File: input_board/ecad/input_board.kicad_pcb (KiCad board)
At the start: 2 copper layers, 165.2 x 98.2 mm, 165 parts, among them J1 Conn_01x03_Male, J10 Conn_01x02_Female, J11 Conn_01x02_Female, J12 Conn_01x02_Female, J13 Conn_01x02_Female, J14 Conn_01x02_Female, J15 Conn_01x02_Female, J2 RCJ-041, J3 RCJ-041, J4 Conn_01x04_Female, J5 Conn_01x02_Female, J6 Conn_01x02_Female, J7 Conn_01x02_Female, J8 Conn_01x02_Female, J9 Conn_01x02_Female, Q1 BC817, Q2 IRFR5305, U1 NJM4580, U10 NJM4580, U11 L7809, U2 MC33079, U3 MC33079, U4 MC33079, U5 NJM4580, U6 MC33079, U7 MC33079, U8 MC33079, U9 MC33079

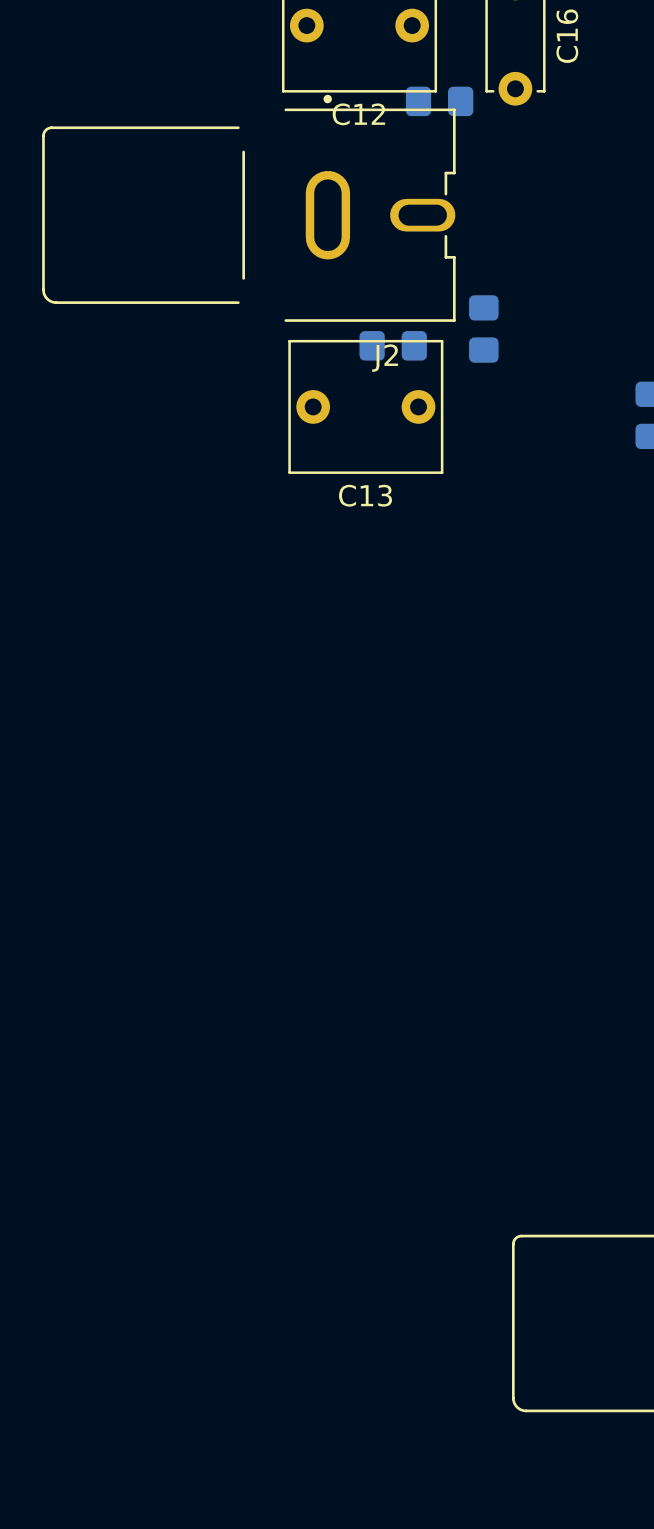
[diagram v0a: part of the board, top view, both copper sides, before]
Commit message: Input board: migrate to KiCAD 6.0
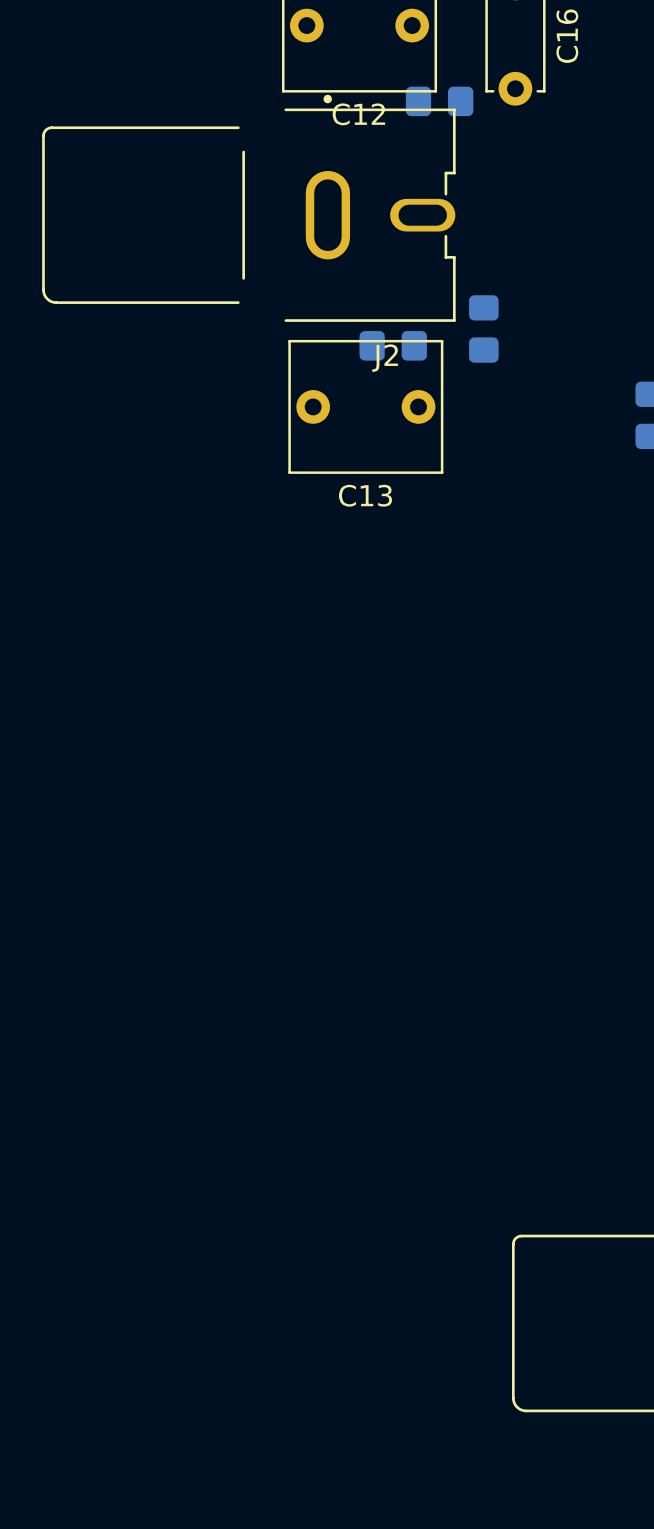
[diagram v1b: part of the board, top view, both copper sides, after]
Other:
- net class Default removed

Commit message: Input board: fix scematic and initial version of layout
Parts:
- removed C34, C36, C38, C39, C40, C41: 100n, Capacitor_SMD:C_0805_2012Metric_Pad1.18x1.45mm_HandSolder
- removed C35, C37: 1n, Capacitor_THT:C_Rect_L7.2mm_W2.5mm_P5.00mm_FKS2_FKP2_MKS2_MKP2
- removed J14, J15: Conn_01x02_Female, Connector_PinHeader_2.54mm:PinHeader_1x02_P2.54mm_Horizontal
- removed R61, R64, R66: 30K, Resistor_SMD:R_0805_2012Metric_Pad1.20x1.40mm_HandSolder
- removed R62, R65, R67, R68, R69, R70, R71, R72, R73, R74, R75, R76, R77, R78: 10K, Resistor_SMD:R_0805_2012Metric_Pad1.20x1.40mm_HandSolder
- removed R63: 7.5K, Resistor_SMD:R_0805_2012Metric_Pad1.20x1.40mm_HandSolder
- removed RV10: 100K, Potentiometer_THT:Potentiometer_Runtron_RM-063_Horizontal
- removed RV11, RV12, RV9: 50K, Potentiometer_THT:Potentiometer_Runtron_RM-063_Horizontal
- removed U10: NJM4580, Package_SO:SOIC-8_3.9x4.9mm_P1.27mm
- removed U11: L7809, Package_TO_SOT_THT:TO-220-3_Horizontal_TabDown
- C10: value 56n -> 100u; footprint Capacitor_THT:C_Rect_L7.0mm_W4.5mm_P5.00mm -> Capacitor_SMD:CP_Elec_6.3x5.7
- C11: value 100n -> 330n
- C13: value 1u -> 10p; footprint Capacitor_THT:C_Rect_L7.0mm_W6.0mm_P5.00mm -> Capacitor_THT:C_Disc_D5.0mm_W2.5mm_P5.00mm
- C15, C25, C26: value 1u -> 1n; footprint Capacitor_THT:C_Rect_L7.0mm_W6.0mm_P5.00mm -> Capacitor_THT:C_Rect_L7.2mm_W2.5mm_P5.00mm_FKS2_FKP2_MKS2_MKP2
- C16: value 10p -> 1n; footprint Capacitor_THT:C_Disc_D5.0mm_W2.5mm_P5.00mm -> Capacitor_THT:C_Rect_L7.2mm_W2.5mm_P5.00mm_FKS2_FKP2_MKS2_MKP2
- C18, C19: value 22n -> 1u; footprint Capacitor_THT:C_Rect_L7.2mm_W2.5mm_P5.00mm_FKS2_FKP2_MKS2_MKP2 -> Capacitor_THT:C_Rect_L7.0mm_W6.0mm_P5.00mm
- C2, C3, C9: value 56n -> 100n; footprint Capacitor_THT:C_Rect_L7.0mm_W4.5mm_P5.00mm -> Capacitor_SMD:C_0805_2012Metric_Pad1.18x1.45mm_HandSolder
- C20, C30, C33: value 47p -> 100n; footprint Capacitor_THT:C_Disc_D5.0mm_W2.5mm_P5.00mm -> Capacitor_SMD:C_0805_2012Metric_Pad1.18x1.45mm_HandSolder; moved to B.Cu
- C21, R10, R22, R34, R37, R38, R39, R45, R46, R5, R51, R55, R6, R60, R7, U7, U8, U9: moved to B.Cu
- C22, C24: value 1n -> 1u; footprint Capacitor_THT:C_Rect_L7.2mm_W2.5mm_P5.00mm_FKS2_FKP2_MKS2_MKP2 -> Capacitor_THT:C_Rect_L7.0mm_W6.0mm_P5.00mm
- C23: value 100n -> 10p; footprint Capacitor_SMD:C_0805_2012Metric_Pad1.18x1.45mm_HandSolder -> Capacitor_THT:C_Disc_D5.0mm_W2.5mm_P5.00mm
- C27: value 1u -> 47p; footprint Capacitor_THT:C_Rect_L7.0mm_W6.0mm_P5.00mm -> Capacitor_THT:C_Disc_D5.0mm_W2.5mm_P5.00mm
- C29: value 10p -> 1u; footprint Capacitor_THT:C_Disc_D5.0mm_W2.5mm_P5.00mm -> Capacitor_THT:C_Rect_L7.0mm_W6.0mm_P5.00mm
- C31, C32: value 22n -> 100n; footprint Capacitor_THT:C_Rect_L7.2mm_W2.5mm_P5.00mm_FKS2_FKP2_MKS2_MKP2 -> Capacitor_SMD:C_0805_2012Metric_Pad1.18x1.45mm_HandSolder; moved to B.Cu
- C4, C7: value 100n -> 56n; footprint Capacitor_SMD:C_0805_2012Metric_Pad1.18x1.45mm_HandSolder -> Capacitor_THT:C_Rect_L7.0mm_W4.5mm_P5.00mm
- C5: value 1000u -> 56n; footprint Capacitor_THT:CP_Radial_D16.0mm_P7.50mm -> Capacitor_THT:C_Rect_L7.0mm_W4.5mm_P5.00mm
- C6: value 330n -> 56n; footprint Capacitor_SMD:C_0805_2012Metric_Pad1.18x1.45mm_HandSolder -> Capacitor_THT:C_Rect_L7.0mm_W4.5mm_P5.00mm
- C8: value 100u -> 1000u; footprint Capacitor_SMD:CP_Elec_6.3x5.7 -> Capacitor_THT:CP_Radial_D16.0mm_P7.50mm
- J1: value Conn_01x03_Male -> Conn_01x02_Female; footprint Connector_Phoenix_MC:PhoenixContact_MC_1,5_3-G-3.5_1x03_P3.50mm_Horizontal -> Connector_PinHeader_2.54mm:PinHeader_1x02_P2.54mm_Horizontal
- J10, J11, J12, J13: footprint Connector_PinHeader_2.54mm:PinHeader_1x02_P2.54mm_Horizontal -> Connector_Phoenix_MC:PhoenixContact_MC_1,5_2-G-3.5_1x02_P3.50mm_Horizontal
- J2: value RCJ-041 -> Conn_01x02_Female; footprint footprints:CUI_RCJ-041 -> Connector_PinHeader_2.54mm:PinHeader_1x02_P2.54mm_Horizontal
- J4: value Conn_01x04_Female -> Conn_01x02_Female; footprint Connector_Phoenix_MC:PhoenixContact_MC_1,5_4-G-3.5_1x04_P3.50mm_Horizontal -> Connector_PinHeader_2.54mm:PinHeader_1x02_P2.54mm_Horizontal
- J5: value Conn_01x02_Female -> Conn_01x04_Female; footprint Connector_Phoenix_MSTB:PhoenixContact_MSTBA_2,5_2-G_1x02_P5.00mm_Horizontal -> Connector_Phoenix_MC:PhoenixContact_MC_1,5_4-G-3.5_1x04_P3.50mm_Horizontal
- J6: value Conn_01x02_Female -> RCJ-041; footprint Connector_Phoenix_MSTB:PhoenixContact_MSTBA_2,5_2-G_1x02_P5.00mm_Horizontal -> footprints:CUI_RCJ-041
- J7, J8: footprint Connector_Phoenix_MSTB:PhoenixContact_MSTBA_2,5_2-G_1x02_P5.00mm_Horizontal -> Connector_PinHeader_2.54mm:PinHeader_1x02_P2.54mm_Horizontal
- J9: value Conn_01x02_Female -> Conn_01x03_Male; footprint Connector_PinHeader_2.54mm:PinHeader_1x02_P2.54mm_Horizontal -> Connector_Phoenix_MC:PhoenixContact_MC_1,5_3-G-3.5_1x03_P3.50mm_Horizontal
- Q1: value BC817 -> IRFR5305; footprint Package_TO_SOT_SMD:SOT-23 -> Package_TO_SOT_SMD:TO-252-2
- Q2: value IRFR5305 -> BC817; footprint Package_TO_SOT_SMD:TO-252-2 -> Package_TO_SOT_SMD:SOT-23
- R12: value 10K -> 4.7K
- R13, R33: value 10K -> 7.5K
- R14, R15, R41, R42: value 10K -> 30K; footprint Resistor_THT:R_Axial_DIN0207_L6.3mm_D2.5mm_P10.16mm_Horizontal -> Resistor_SMD:R_0805_2012Metric_Pad1.20x1.40mm_HandSolder; moved to B.Cu
- R16: value 4.7K -> 10K; footprint Resistor_THT:R_Axial_DIN0207_L6.3mm_D2.5mm_P10.16mm_Horizontal -> Resistor_SMD:R_0805_2012Metric_Pad1.20x1.40mm_HandSolder; moved to B.Cu
- R17, R21, R35, R40: value 10K -> 30K; moved to B.Cu
- R18, R27, R47, R49, R54, R57, R59: value 30K -> 10K; moved to B.Cu
- R24: value 30K -> 4.7K
- R25: value 7.5K -> 30K; moved to B.Cu
- R26, R31: value 18K -> 30K; moved to B.Cu
- R28, R48: footprint Resistor_SMD:R_0805_2012Metric_Pad1.20x1.40mm_HandSolder -> Resistor_THT:R_Axial_DIN0207_L6.3mm_D2.5mm_P10.16mm_Horizontal
- R29, R3, R56: value 4.7K -> 10K; moved to B.Cu
- R30: value 30K -> 4.7K; footprint Resistor_SMD:R_0805_2012Metric_Pad1.20x1.40mm_HandSolder -> Resistor_THT:R_Axial_DIN0207_L6.3mm_D2.5mm_P10.16mm_Horizontal; moved to F.Cu
- R32: value 30K -> 10K; footprint Resistor_SMD:R_0805_2012Metric_Pad1.20x1.40mm_HandSolder -> Resistor_THT:R_Axial_DIN0207_L6.3mm_D2.5mm_P10.16mm_Horizontal
- R36: value 7.5K -> 10K; moved to B.Cu
- R4: value 10K -> 20K; moved to B.Cu
- R43: value 4.7K -> 30K; footprint Resistor_THT:R_Axial_DIN0207_L6.3mm_D2.5mm_P10.16mm_Horizontal -> Resistor_SMD:R_0805_2012Metric_Pad1.20x1.40mm_HandSolder; moved to B.Cu
- R44: value 10K -> 4.7K; moved to B.Cu
- R50: value 30K -> 4.7K; footprint Resistor_SMD:R_0805_2012Metric_Pad1.20x1.40mm_HandSolder -> Resistor_THT:R_Axial_DIN0207_L6.3mm_D2.5mm_P10.16mm_Horizontal
- R52: value 7.5K -> 10K; footprint Resistor_SMD:R_0805_2012Metric_Pad1.20x1.40mm_HandSolder -> Resistor_THT:R_Axial_DIN0207_L6.3mm_D2.5mm_P10.16mm_Horizontal
- R53, R58: value 18K -> 10K; moved to B.Cu
- R8: value 20K -> 5.8K; moved to B.Cu
- R9: value 5.8K -> 10K; moved to B.Cu
- RV3, RV5, RV8: value 100K -> 50K
- U1: value NJM4580 -> LM358
- U3: value MC33079 -> L7809; footprint Package_SO:SOIC-14_3.9x8.7mm_P1.27mm -> Package_TO_SOT_THT:TO-220-3_Horizontal_TabDown
- U4, U6: value MC33079 -> NJM4580; footprint Package_SO:SOIC-14_3.9x8.7mm_P1.27mm -> Package_SO:SOIC-8_3.9x4.9mm_P1.27mm; moved to B.Cu
- U5: value NJM4580 -> MC33079; footprint Package_SO:SOIC-8_3.9x4.9mm_P1.27mm -> Package_SO:SOIC-14_3.9x8.7mm_P1.27mm; moved to B.Cu
- moved R48 228.0 mm to (40.1, 30.5), turned to 180 degrees
- moved R50 217.9 mm to (42.0, 38.8)
- moved R52 215.0 mm to (40.1, 34.5), turned to 180 degrees
- moved R41 203.2 mm to (35.5, 66.2), turned to 180 degrees
- moved R44 203.0 mm to (61.8, 41.5), turned to 180 degrees
- moved C28 200.5 mm to (56.0, 33.8), turned to 180 degrees
- moved R46 195.3 mm to (64.8, 49.8)
- moved R57 193.2 mm to (81.2, 57.1), turned to -90 degrees
- moved R45 192.4 mm to (59.2, 51.5)
- moved C29 190.5 mm to (47.8, 33.8), turned to 180 degrees
- moved R3 190.2 mm to (33.5, 90.6), turned to -90 degrees
- moved R40 185.0 mm to (76.0, 84.3), turned to -90 degrees
- moved RV8 184.1 mm to (68.1, 86.3), turned to 90 degrees
- moved R47 180.1 mm to (74.2, 75.8), turned to 90 degrees
- moved C27 178.4 mm to (70.2, 78.3), turned to 90 degrees
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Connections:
- C10 pad 1: Net-(C10-Pad1) -> +9V
- C10 pad 2: Net-(C10-Pad2) -> GND
- C11 pad 1: +9V -> /VCC_BRFORE_STAB
- C12 pad 2: /preamp_filter_r/rca_n -> /left_rca_p
- C13 pad 1: Net-(C13-Pad1) -> /preamp_filter_l/preamp_n
- C13 pad 2: /preamp_filter_r/rca_p -> /preamp_filter_l/preamp_p
- C14 pad 2: Net-(C14-Pad2) -> /left_rca_g
- C16 pad 1: Net-(C16-Pad1) -> /preamp_filter_l/LO_MID
- C17 pad 1: /preamp_filter_r/MID -> /preamp_filter_l/HIGH
- C19 pad 1: /preamp_filter_r/LOW -> Net-(C19-Pad1)
- C2 pad 1: Net-(C2-Pad1) -> +9V
- C2 pad 2: Net-(C2-Pad2) -> GND
- C20 pad 1: /preamp_filter_r/HIGH -> +9V
- C20 pad 2: Net-(C20-Pad2) -> GND
- C22 pad 2: Net-(C22-Pad2) -> /right_rca_p
- C23 pad 1: +9V -> /preamp_filter_r/preamp_n
- C23 pad 2: GND -> /preamp_filter_r/preamp_p
- C24 pad 1: /preamp_filter_r/LO_MID -> Net-(C24-Pad1)
- C24 pad 2: Net-(C24-Pad2) -> /right_rca_g
- C25 pad 2: /preamp_filter_l/rca_n -> Net-(C25-Pad2)
- C26 pad 1: Net-(C26-Pad1) -> /preamp_filter_r/LO_MID
- C26 pad 2: /preamp_filter_l/rca_p -> Net-(C26-Pad2)
- C27 pad 1: Net-(C27-Pad1) -> /preamp_filter_r/HIGH
- C3 pad 1: Net-(C2-Pad2) -> Net-(C3-Pad1)
- C3 pad 2: Net-(C3-Pad2) -> GND
- C30 pad 1: /preamp_filter_l/MID -> +9V
- C30 pad 2: Net-(C30-Pad2) -> GND
- C31 pad 1: Net-(C31-Pad1) -> +9V
- C31 pad 2: Net-(C31-Pad2) -> GND
- C32 pad 1: /preamp_filter_l/LOW -> +9V
- C32 pad 2: Net-(C32-Pad2) -> GND
- C33 pad 1: /preamp_filter_l/HIGH -> +9V
- C33 pad 2: Net-(C33-Pad2) -> GND
- C4 pad 2: GND -> Net-(C4-Pad2)
- C5 pad 1: vcc_prefiltered -> Net-(C5-Pad1)
- C5 pad 2: GND -> half_vcc
- C6 pad 1: Net-(C6-Pad1) -> /VCC_UNFILTERED
- C6 pad 2: GND -> Net-(C6-Pad2)
- C7 pad 1: +9V -> Net-(C6-Pad2)
- C7 pad 2: GND -> /GND_DIRTY
- C8 pad 1: +9V -> vcc_prefiltered
- C9 pad 1: Net-(C9-Pad1) -> +9V
- C9 pad 2: half_vcc -> GND
- D1 pad 1: Net-(C2-Pad1) -> /VCC_UNFILTERED
- D2 pad 1: Net-(C3-Pad2) -> /GND_DIRTY
- D3 pad 1: Net-(D3-Pad1) -> /ENABLE
- D4 pad 1: Net-(C3-Pad2) -> /GND_DIRTY
- FL1 pad 1: Net-(C3-Pad2) -> /GND_DIRTY
- FL1 pad 2: Net-(FL1-Pad2) -> /VCC_UNF_EN
- J1 pad 1: Net-(C2-Pad1) -> /se_to_diff_r/HI_P
- J1 pad 2: Net-(C3-Pad2) -> /se_to_diff_r/HI_N
- J10 pad 1: /se_to_diff_l/MID_P -> vcc_prefiltered
- J10 pad 2: /se_to_diff_l/MID_N -> GND
- J11 pad 1: /se_to_diff_l/LOW_P -> vcc_prefiltered
- J11 pad 2: /se_to_diff_l/LOW_N -> GND
- J12 pad 1: /se_to_diff_r/HI_P -> vcc_prefiltered
- J12 pad 2: /se_to_diff_r/HI_N -> GND
- J13 pad 1: /se_to_diff_r/MID_P -> vcc_prefiltered
- J13 pad 2: /se_to_diff_r/MID_N -> GND
- J2 pad 1: /preamp_filter_r/rca_p -> /se_to_diff_r/LOMID_P
- J2 pad 2: /preamp_filter_r/rca_n -> /se_to_diff_r/LOMID_N
- J3 pad 1: /preamp_filter_l/rca_p -> /right_rca_g
- J3 pad 2: /preamp_filter_l/rca_n -> /right_rca_p
- J4 pad 1: /preamp_filter_l/hi_n -> /lfe_p
- J4 pad 2: /preamp_filter_l/hi_p -> /lfe_n
- J5 pad 1: vcc_prefiltered -> /preamp_filter_l/hi_n
- J5 pad 2: GND -> /preamp_filter_l/hi_p
- J6 pad 1: vcc_prefiltered -> /left_rca_g
- J6 pad 2: GND -> /left_rca_p
- J7 pad 1: vcc_prefiltered -> /se_to_diff_l/HI_P
- J7 pad 2: GND -> /se_to_diff_l/HI_N
- J8 pad 1: vcc_prefiltered -> /se_to_diff_l/LOMID_P
- J8 pad 2: GND -> /se_to_diff_l/LOMID_N
- J9 pad 1: /se_to_diff_l/HI_P -> /VCC_UNFILTERED
- J9 pad 2: /se_to_diff_l/HI_N -> /GND_DIRTY
- L1 pad 2: Net-(C6-Pad1) -> /VCC_BRFORE_STAB
- Q1 pad 2: Net-(C3-Pad2) -> /VCC_UNF_EN
- Q1 pad 3: Net-(Q1-Pad3) -> /VCC_UNFILTERED
- Q2 pad 1: Net-(Q1-Pad3) -> Net-(Q2-Pad1)
- Q2 pad 2: Net-(FL1-Pad2) -> /GND_DIRTY
- Q2 pad 3: Net-(C2-Pad1) -> Net-(Q1-Pad1)
- R1 pad 2: Net-(C4-Pad1) -> Net-(C3-Pad1)
- R11 pad 1: Net-(R11-Pad1) -> Net-(Q1-Pad1)
- R11 pad 2: Net-(R10-Pad1) -> /VCC_UNFILTERED
- R12 pad 1: /lfe_p -> /ENABLE
- R12 pad 2: Net-(R11-Pad1) -> Net-(Q2-Pad1)
- R13 pad 1: /preamp_filter_r/rca_n -> Net-(C15-Pad1)
- R13 pad 2: /preamp_filter_r/rca_p -> Net-(R13-Pad2)
- R14 pad 1: Net-(C14-Pad2) -> /preamp_filter_l/preamp_p
- R14 pad 2: /preamp_filter_r/hi_p -> half_vcc
- R15 pad 1: Net-(C15-Pad2) -> /preamp_filter_l/preamp_p
- R15 pad 2: /preamp_filter_r/hi_n -> Net-(C12-Pad1)
- R16 pad 1: Net-(C15-Pad2) -> Net-(R13-Pad2)
- R16 pad 2: Net-(C14-Pad2) -> Net-(R16-Pad2)
- R17 pad 1: Net-(R17-Pad1) -> Net-(C16-Pad2)
- R17 pad 2: /preamp_filter_r/LO_MID -> Net-(R17-Pad2)
- R18 pad 1: half_vcc -> /left_rca_p
- R18 pad 2: Net-(C17-Pad2) -> /left_rca_g
- R19 pad 1: Net-(C16-Pad2) -> Net-(R19-Pad1)
- R19 pad 2: Net-(C12-Pad1) -> Net-(R19-Pad2)
- R2 pad 1: Net-(C4-Pad1) -> Net-(C3-Pad1)
- R20 pad 1: Net-(C16-Pad1) -> Net-(C15-Pad2)
- R20 pad 2: Net-(C13-Pad1) -> Net-(R20-Pad2)
- R21 pad 1: /preamp_filter_r/MID -> /preamp_filter_l/preamp_n
- R21 pad 2: Net-(C17-Pad2) -> Net-(C14-Pad1)
- R22 pad 1: Net-(C14-Pad1) -> Net-(R22-Pad1)
- R22 pad 2: Net-(C16-Pad1) -> /preamp_filter_l/preamp_n
- R23 pad 1: Net-(C16-Pad2) -> Net-(R16-Pad2)
- R23 pad 2: half_vcc -> Net-(R19-Pad1)
- R24 pad 1: Net-(C15-Pad1) -> half_vcc
- R24 pad 2: Net-(C16-Pad2) -> Net-(R24-Pad2)
- R25 pad 2: Net-(R17-Pad1) -> /preamp_filter_l/preamp_n
- R26 pad 1: Net-(C18-Pad2) -> Net-(C19-Pad1)
- R26 pad 2: Net-(R26-Pad2) -> /preamp_filter_l/preamp_p
- R27 pad 1: Net-(R27-Pad1) -> /preamp_filter_l/HIGH
- R27 pad 2: Net-(C16-Pad1) -> Net-(C17-Pad2)
- R28 pad 1: /preamp_filter_r/LOW -> Net-(C18-Pad2)
- R28 pad 2: Net-(C17-Pad2) -> /preamp_filter_l/hi_n
- R29 pad 1: half_vcc -> /preamp_filter_l/LO_MID
- R29 pad 2: Net-(R29-Pad2) -> Net-(C17-Pad2)
- R3 pad 1: Net-(D3-Pad1) -> /preamp_filter_r/LO_MID
- R3 pad 2: Net-(Q1-Pad1) -> Net-(R3-Pad2)
- R30 pad 1: Net-(R30-Pad1) -> Net-(C19-Pad2)
- R30 pad 2: Net-(R30-Pad2) -> Net-(C18-Pad2)
- R31 pad 1: Net-(C19-Pad2) -> half_vcc
- R31 pad 2: Net-(R31-Pad2) -> Net-(C17-Pad2)
- R32 pad 1: Net-(R32-Pad1) -> Net-(C19-Pad2)
- R32 pad 2: Net-(R30-Pad1) -> /preamp_filter_l/hi_p
- R33 pad 1: Net-(R33-Pad1) -> Net-(C25-Pad1)
- R33 pad 2: Net-(R32-Pad1) -> Net-(R33-Pad2)
- R34 pad 1: half_vcc -> /preamp_filter_r/preamp_p
- R34 pad 2: Net-(C20-Pad2) -> half_vcc
- R35 pad 1: /preamp_filter_r/HIGH -> /preamp_filter_r/preamp_p
- R35 pad 2: Net-(C20-Pad2) -> Net-(C22-Pad1)
- R36 pad 1: Net-(C22-Pad1) -> Net-(R33-Pad2)
- R36 pad 2: Net-(R33-Pad1) -> Net-(R36-Pad2)
- R37 pad 1: Net-(C22-Pad2) -> Net-(C26-Pad2)
- R38 pad 1: /preamp_filter_r/LO_MID -> /right_rca_p
- R38 pad 2: Net-(C20-Pad2) -> /right_rca_g
- R39 pad 1: Net-(C24-Pad2) -> Net-(R39-Pad1)
- R4 pad 1: Net-(Q1-Pad3) -> Net-(C5-Pad1)
- R4 pad 2: Net-(C2-Pad1) -> Net-(R4-Pad2)
- R40 pad 1: /preamp_filter_l/rca_n -> Net-(C25-Pad2)
- R40 pad 2: /preamp_filter_l/rca_p -> Net-(R40-Pad2)
- R41 pad 1: Net-(C27-Pad2) -> /preamp_filter_r/preamp_n
- R41 pad 2: /preamp_filter_l/hi_p -> Net-(C24-Pad1)
- R42 pad 1: Net-(C28-Pad2) -> Net-(R42-Pad1)
- R42 pad 2: /preamp_filter_l/hi_n -> /preamp_filter_r/preamp_n
- R43 pad 1: Net-(C28-Pad2) -> Net-(R36-Pad2)
- R43 pad 2: Net-(C27-Pad2) -> Net-(R39-Pad1)
- R44 pad 1: Net-(R44-Pad1) -> half_vcc
- R44 pad 2: /preamp_filter_l/LO_MID -> Net-(R44-Pad2)
- R45 pad 1: half_vcc -> Net-(C28-Pad1)
- R45 pad 2: Net-(C30-Pad2) -> /preamp_filter_r/preamp_n
- R46 pad 1: Net-(C29-Pad2) -> Net-(C29-Pad1)
- R46 pad 2: Net-(C25-Pad1) -> /preamp_filter_r/preamp_p
- R47 pad 1: Net-(C29-Pad1) -> /preamp_filter_r/HIGH
- R47 pad 2: Net-(C26-Pad1) -> Net-(C27-Pad2)
- R48 pad 1: /preamp_filter_l/MID -> Net-(C28-Pad2)
- R48 pad 2: Net-(C30-Pad2) -> /preamp_filter_r/hi_n
- R49 pad 1: Net-(C27-Pad1) -> /preamp_filter_r/LO_MID
- R49 pad 2: Net-(C29-Pad1) -> Net-(C27-Pad2)
- R5 pad 1: /preamp_filter_r/LO_MID -> Net-(R5-Pad1)
- R5 pad 2: Net-(R5-Pad2) -> Net-(R10-Pad1)
- R50 pad 2: half_vcc -> Net-(C28-Pad2)
- R51 pad 1: Net-(C28-Pad1) -> half_vcc
- R51 pad 2: Net-(C29-Pad2) -> Net-(C27-Pad2)
- R52 pad 1: Net-(C31-Pad1) -> Net-(C29-Pad2)
- R52 pad 2: Net-(R44-Pad1) -> /preamp_filter_r/hi_p
- R53 pad 1: Net-(C31-Pad2) -> Net-(R53-Pad1)
- R53 pad 2: Net-(R53-Pad2) -> /preamp_filter_l/HIGH
- R54 pad 1: Net-(R54-Pad1) -> /se_to_diff_l/HI_P
- R54 pad 2: Net-(C29-Pad1) -> Net-(R53-Pad1)
- R55 pad 1: /preamp_filter_l/LOW -> Net-(R55-Pad1)
- R55 pad 2: Net-(C30-Pad2) -> /preamp_filter_l/LO_MID
- R56 pad 1: half_vcc -> /se_to_diff_l/LOMID_N
- R56 pad 2: Net-(R56-Pad2) -> Net-(R55-Pad1)
- R57 pad 2: Net-(R57-Pad2) -> /preamp_filter_r/HIGH
- R58 pad 1: Net-(C32-Pad2) -> /se_to_diff_r/HI_P
- R58 pad 2: Net-(R58-Pad2) -> Net-(R57-Pad1)
- R59 pad 2: Net-(R57-Pad1) -> /preamp_filter_r/LO_MID
- R6 pad 1: Net-(R5-Pad2) -> /lfe_p
- R6 pad 2: /preamp_filter_l/LO_MID -> Net-(R5-Pad1)
- R60 pad 1: Net-(R60-Pad1) -> /se_to_diff_r/LOMID_N
- R7 pad 1: Net-(C10-Pad2) -> Net-(C4-Pad2)
- R8 pad 1: Net-(C9-Pad1) -> Net-(C4-Pad1)
- R8 pad 2: Net-(R8-Pad2) -> Net-(R10-Pad1)
- R9 pad 1: Net-(C10-Pad1) -> Net-(R3-Pad2)
- R9 pad 2: Net-(R10-Pad1) -> /preamp_filter_l/LO_MID
- RV1 pad 1: Net-(R5-Pad2) -> Net-(C4-Pad2)
- RV1 pad 2: Net-(R5-Pad2) -> Net-(C4-Pad2)
- RV1 pad 3: Net-(R7-Pad2) -> Net-(R4-Pad2)
- RV2 pad 1: Net-(C10-Pad2) -> Net-(R3-Pad2)
- RV2 pad 2: Net-(C10-Pad2) -> Net-(R3-Pad2)
- RV2 pad 3: Net-(R8-Pad2) -> Net-(R7-Pad2)
- RV3 pad 1: Net-(R26-Pad2) -> Net-(R17-Pad2)
- RV3 pad 2: /preamp_filter_r/MID -> Net-(C15-Pad1)
- RV3 pad 3: /preamp_filter_r/MID -> Net-(C15-Pad1)
- RV4 pad 1: Net-(R27-Pad1) -> Net-(R22-Pad1)
- RV4 pad 2: Net-(R30-Pad2) -> Net-(R19-Pad2)
- RV4 pad 3: Net-(R29-Pad2) -> Net-(R24-Pad2)
- RV5 pad 1: Net-(R31-Pad2) -> Net-(R20-Pad2)
- RV5 pad 2: Net-(C18-Pad1) -> /preamp_filter_l/HIGH
- RV5 pad 3: Net-(C18-Pad1) -> /preamp_filter_l/HIGH
- RV6 pad 2: /preamp_filter_r/HIGH -> Net-(C25-Pad1)
- RV6 pad 3: /preamp_filter_r/HIGH -> Net-(C25-Pad1)
- RV7 pad 1: Net-(R39-Pad2) -> Net-(R42-Pad1)
- RV7 pad 2: Net-(C22-Pad1) -> Net-(R39-Pad2)
- RV7 pad 3: Net-(C22-Pad1) -> Net-(R44-Pad2)
- RV8 pad 1: Net-(R53-Pad2) -> Net-(R40-Pad2)
- RV8 pad 2: /preamp_filter_l/MID -> /preamp_filter_r/HIGH
- RV8 pad 3: /preamp_filter_l/MID -> /preamp_filter_r/HIGH
- U1 pad 3: Net-(C4-Pad1) -> Net-(C3-Pad1)
- U2 pad 1: Net-(R27-Pad1) -> Net-(C4-Pad1)
- U2 pad 10: Net-(R33-Pad1) -> Net-(R10-Pad1)
- U2 pad 12: half_vcc -> (no net)
- U2 pad 13: Net-(C22-Pad2) -> (no net)
- U2 pad 14: Net-(C22-Pad1) -> (no net)
- U2 pad 2: Net-(C16-Pad1) -> Net-(R10-Pad1)
- U2 pad 3: Net-(C16-Pad2) -> Net-(C5-Pad1)
- U2 pad 6: Net-(R30-Pad1) -> Net-(R5-Pad1)
- U2 pad 7: Net-(R32-Pad1) -> /lfe_p
- U2 pad 8: /preamp_filter_r/HIGH -> /lfe_n
- U2 pad 9: Net-(C20-Pad2) -> /lfe_n
- U3 pad 1: /preamp_filter_r/LO_MID -> /VCC_BRFORE_STAB
- U3 pad 2: Net-(C24-Pad2) -> GND
- U3 pad 3: half_vcc -> +9V
- U4 pad 1: /se_to_diff_r/HI_N -> Net-(R22-Pad1)
- U4 pad 2: /se_to_diff_r/HI_N -> /preamp_filter_l/preamp_n
- U4 pad 3: /preamp_filter_r/HIGH -> /preamp_filter_l/preamp_p
- U4 pad 4: +9V -> GND
- U4 pad 6: Net-(R68-Pad1) -> Net-(R19-Pad1)
- U4 pad 7: /se_to_diff_r/HI_P -> Net-(R16-Pad2)
- U4 pad 8: /se_to_diff_r/MID_N -> +9V
- U5 pad 1: /se_to_diff_r/LOW_P -> (no net)
- U5 pad 2: Net-(R67-Pad1) -> (no net)
- U5 pad 3: half_vcc -> (no net)
- U5 pad 4: GND -> +9V
- U5 pad 5: /preamp_filter_r/LOW -> half_vcc
- U5 pad 6: /se_to_diff_r/LOW_N -> Net-(C16-Pad2)
- U5 pad 7: /se_to_diff_r/LOW_N -> /preamp_filter_l/LO_MID
- U5 pad 8: +9V -> /preamp_filter_l/HIGH
- U6 pad 1: Net-(C10-Pad1) -> Net-(R42-Pad1)
- U6 pad 2: Net-(R10-Pad1) -> /preamp_filter_r/preamp_n
- U6 pad 3: Net-(C9-Pad1) -> /preamp_filter_r/preamp_p
- U6 pad 4: +9V -> GND
- U6 pad 6: Net-(R11-Pad1) -> Net-(R39-Pad1)
- U6 pad 7: /lfe_p -> Net-(R36-Pad2)
- U6 pad 8: /lfe_n -> +9V
- U7 pad 1: Net-(R54-Pad1) -> (no net)
- U7 pad 10: Net-(R60-Pad1) -> Net-(R33-Pad2)
- U7 pad 13: Net-(C35-Pad2) -> Net-(C25-Pad2)
- U7 pad 14: Net-(C35-Pad1) -> Net-(C25-Pad1)
- U7 pad 2: Net-(C29-Pad1) -> (no net)
- U7 pad 3: Net-(C29-Pad2) -> (no net)
- U7 pad 6: Net-(R57-Pad1) -> Net-(C26-Pad2)
- U7 pad 7: Net-(R59-Pad1) -> /preamp_filter_r/LO_MID
- U7 pad 8: /preamp_filter_l/HIGH -> /preamp_filter_r/HIGH
- U7 pad 9: Net-(C33-Pad2) -> Net-(C27-Pad2)
- U8 pad 1: /preamp_filter_l/LO_MID -> /se_to_diff_l/HI_N
- U8 pad 12: half_vcc -> /preamp_filter_l/LO_MID
- U8 pad 13: Net-(C32-Pad2) -> /se_to_diff_l/LOMID_P
- U8 pad 14: /preamp_filter_l/LOW -> /se_to_diff_l/LOMID_P
- U8 pad 2: Net-(C37-Pad2) -> /se_to_diff_l/HI_N
- U8 pad 3: half_vcc -> /preamp_filter_l/HIGH
- U8 pad 5: Net-(R44-Pad1) -> half_vcc
- U8 pad 6: Net-(C30-Pad2) -> Net-(R53-Pad1)
- U8 pad 7: /preamp_filter_l/MID -> /se_to_diff_l/HI_P
- U8 pad 8: Net-(C31-Pad1) -> /se_to_diff_l/LOMID_N
- U8 pad 9: Net-(C31-Pad2) -> Net-(R55-Pad1)
- U9 pad 1: /se_to_diff_l/HI_N -> /se_to_diff_r/HI_N
- U9 pad 12: /preamp_filter_l/MID -> /preamp_filter_r/LO_MID
- U9 pad 13: /se_to_diff_l/MID_P -> /se_to_diff_r/LOMID_P
- U9 pad 14: /se_to_diff_l/MID_P -> /se_to_diff_r/LOMID_P
- U9 pad 2: /se_to_diff_l/HI_N -> /se_to_diff_r/HI_N
- U9 pad 3: /preamp_filter_l/HIGH -> /preamp_filter_r/HIGH
- U9 pad 6: Net-(R74-Pad1) -> Net-(R57-Pad1)
- U9 pad 7: /se_to_diff_l/HI_P -> /se_to_diff_r/HI_P
- U9 pad 8: /se_to_diff_l/MID_N -> /se_to_diff_r/LOMID_N
- U9 pad 9: Net-(R75-Pad1) -> Net-(R59-Pad1)
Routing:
- net +9V: track 0.00 -> 230.8 mm, vias 0 -> 8
- net GND: track 0.00 -> 230.2 mm, vias 0 -> 11
- net half_vcc: track 6.50 -> 213.4 mm, vias 0 -> 12
- net /preamp_filter_r/LO_MID: track 0.00 -> 105.7 mm, vias 0 -> 2
- net /preamp_filter_l/LO_MID: track 0.00 -> 105.0 mm, vias 0 -> 3
- net /preamp_filter_l/HIGH: track 0.00 -> 92.8 mm
- net /preamp_filter_r/preamp_p: track 0.00 -> 54.2 mm, vias 0 -> 2
- net /preamp_filter_r/HIGH: track 0.00 -> 53.0 mm, vias 0 -> 3
- net /lfe_n: track 0.00 -> 52.5 mm, vias 0 -> 1
- net Net-(R33-Pad2): track 0.00 -> 48.1 mm
- net /preamp_filter_r/preamp_n: track 0.00 -> 46.4 mm
- net /lfe_p: track 0.00 -> 45.4 mm
- net /preamp_filter_l/preamp_p: track 0.00 -> 44.6 mm
- net Net-(C17-Pad2): track 0.00 -> 42.7 mm, vias 0 -> 1
- net Net-(C27-Pad2): track 0.00 -> 41.3 mm, vias 0 -> 1
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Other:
- board size 165.2 x 98.2 mm -> 90 x 100 mm
